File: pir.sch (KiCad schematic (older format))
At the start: 10 parts, among them J6 Conn_01x03_Male, J7 Conn_01x03_Male, Q6 BC817

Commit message: started pcb routing
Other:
- note added: "Setup I) AM312 direct connection | default"
- note removed: "Setup I) AM312 direct connection"
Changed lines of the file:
@@
 	5750 2250 5400 2250
 Connection ~ 5400 2250
-Text Notes 3150 2450 0    50   ~ 0
-Setup I)  AM312 direct connection
-Text Notes 3150 2300 0    50   ~ 10
+Text Notes 2890 2810 0    50   ~ 0
+Setup I)  AM312 direct connection | default
+Text Notes 2890 2660 0    50   ~ 10
 Note:
-Text Notes 3150 2550 0    50   ~ 0
+Text Notes 2890 2910 0    50   ~ 0
 Setup II) Transistor connection
 $Comp
@@
 Wire Wire Line
 	4800 3250 4550 3250
-Text Notes 6050 2600 0    50   ~ 10
+Text Notes 6070 2670 0    50   ~ 10
 AM312\n
 $Comp

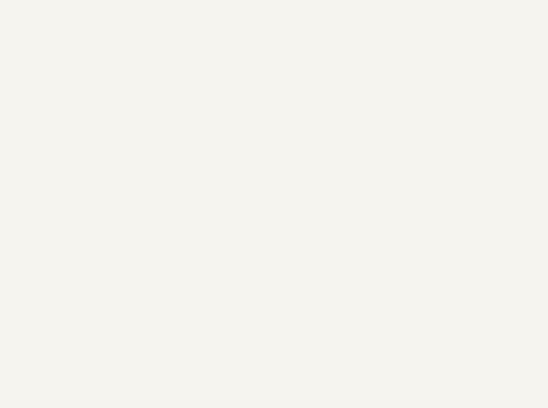
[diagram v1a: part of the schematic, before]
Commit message: layout and more silk informations
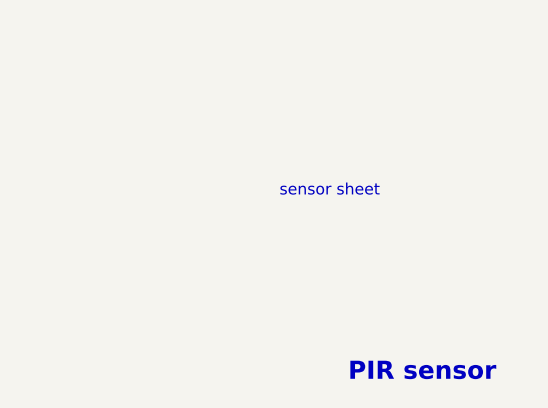
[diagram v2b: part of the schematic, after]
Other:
- note added: "PIR sensor"
- note added: "sensor sheet"
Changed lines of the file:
@@
 Text HLabel 4600 5350 0    50   Output ~ 0
 ldr_sense
+Text Notes 7350 7510 0    79   ~ 16
+PIR sensor
+Text Notes 7050 6700 0    50   ~ 0
+sensor sheet
 $EndSCHEMATC

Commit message: finished layout, created production files and added readme
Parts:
- C6: LCSC (none) -> C13585; MPN (none) -> CL31A106KBHNNNE
- C7, C8: LCSC (none) -> C28233; MPN (none) -> CL21B104KCFNNNE
- R25: LCSC (none) -> C17513; MPN (none) -> 0805W8F1001T5E
- R26: LCSC (none) -> C17407; MPN (none) -> 0805W8F1003T5E
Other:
- note added: "1.0"
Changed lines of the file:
@@
 F 2 "Capacitor_SMD:C_1210_3225Metric_Pad1.42x2.65mm_HandSolder" H 5038 2350 50  0001 C CNN
 F 3 "~" H 5000 2500 50  0001 C CNN
+F 4 "CL31A106KBHNNNE" H 5000 2500 50  0001 C CNN "MPN"
+F 5 "C13585" H 5000 2500 50  0001 C CNN "LCSC"
 	1    5000 2500
 	1    0    0    -1
@@
 F 2 "Capacitor_SMD:C_0805_2012Metric_Pad1.15x1.40mm_HandSolder" H 5438 2350 50  0001 C CNN
 F 3 "~" H 5400 2500 50  0001 C CNN
+F 4 "CL21B104KCFNNNE" H 5400 2500 50  0001 C CNN "MPN"
+F 5 "C28233" H 5400 2500 50  0001 C CNN "LCSC"
 	1    5400 2500
 	-1   0    0    1
@@
 F 2 "Resistor_SMD:R_0805_2012Metric_Pad1.15x1.40mm_HandSolder" V 5380 3850 50  0001 C CNN
 F 3 "~" H 5450 3850 50  0001 C CNN
+F 4 "0805W8F1001T5E" H 5450 3850 50  0001 C CNN "MPN"
+F 5 "C17513" H 5450 3850 50  0001 C CNN "LCSC"
 	1    5450 3850
 	0    -1   -1   0
@@
 F 2 "Capacitor_SMD:C_0805_2012Metric_Pad1.15x1.40mm_HandSolder" H 5088 5550 50  0001 C CNN
 F 3 "~" H 5050 5700 50  0001 C CNN
+F 4 "CL21B104KCFNNNE" H 5050 5700 50  0001 C CNN "MPN"
+F 5 "C28233" H 5050 5700 50  0001 C CNN "LCSC"
 	1    5050 5700
 	-1   0    0    1
@@
 F 2 "Resistor_SMD:R_0805_2012Metric_Pad1.15x1.40mm_HandSolder" V 5380 5700 50  0001 C CNN
 F 3 "~" H 5450 5700 50  0001 C CNN
+F 4 "0805W8F1003T5E" H 5450 5700 50  0001 C CNN "MPN"
+F 5 "C17407" H 5450 5700 50  0001 C CNN "LCSC"
 	1    5450 5700
 	1    0    0    -1
@@
 Text Notes 7050 6700 0    50   ~ 0
 sensor sheet
+Text Notes 10580 7640 0    50   ~ 0
+1.0
 $EndSCHEMATC
